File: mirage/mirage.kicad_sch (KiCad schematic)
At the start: 9 parts, among them U1 STM32H573ZITx

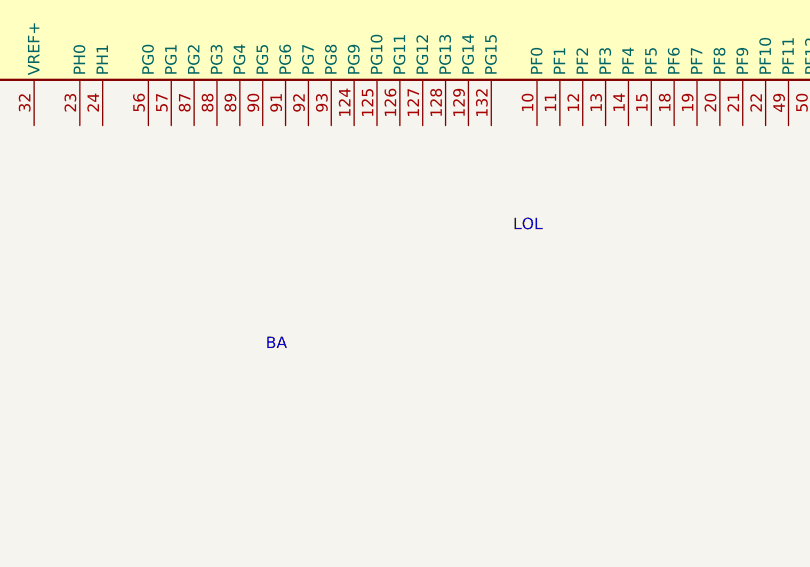
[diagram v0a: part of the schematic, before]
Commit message: feat: add red LED
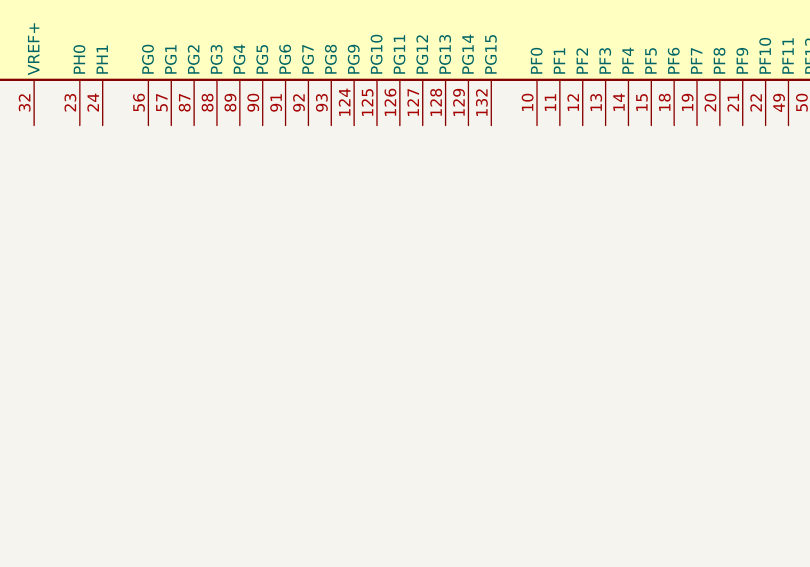
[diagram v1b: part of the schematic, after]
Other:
- note removed: "BA"
- note removed: "LOL"

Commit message: feat: add some text
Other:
- note added: "LOL"
